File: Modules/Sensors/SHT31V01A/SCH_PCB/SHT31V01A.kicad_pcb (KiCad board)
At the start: 2 copper layers, 40.1 x 9.7 mm, 18 parts, among them J1 CONN1_1, J10 JUMP_2x1, J11 JUMP_2x1, J12 JUMP_2x1, J13 JUMP_2x1, J2 CONN1_1, J9 JUMP_2x1, M1 HOLE, M2 HOLE, U1 SHT31

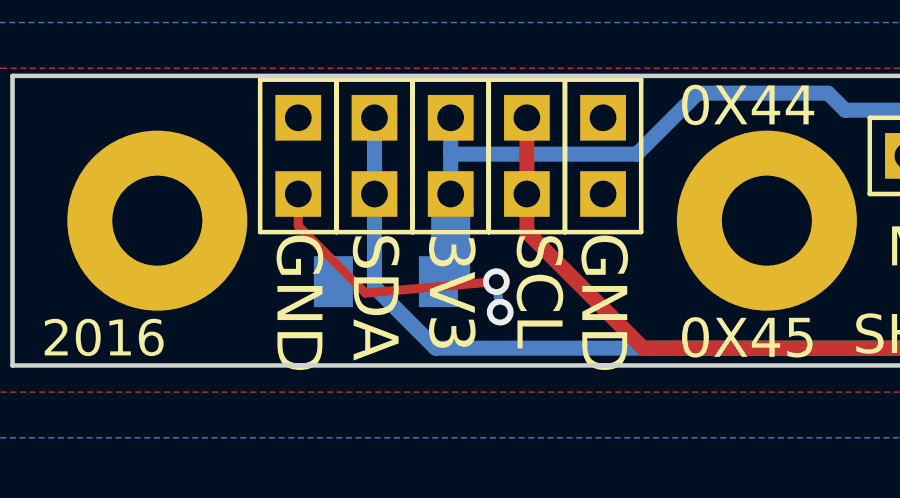
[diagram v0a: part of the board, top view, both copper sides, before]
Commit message: 
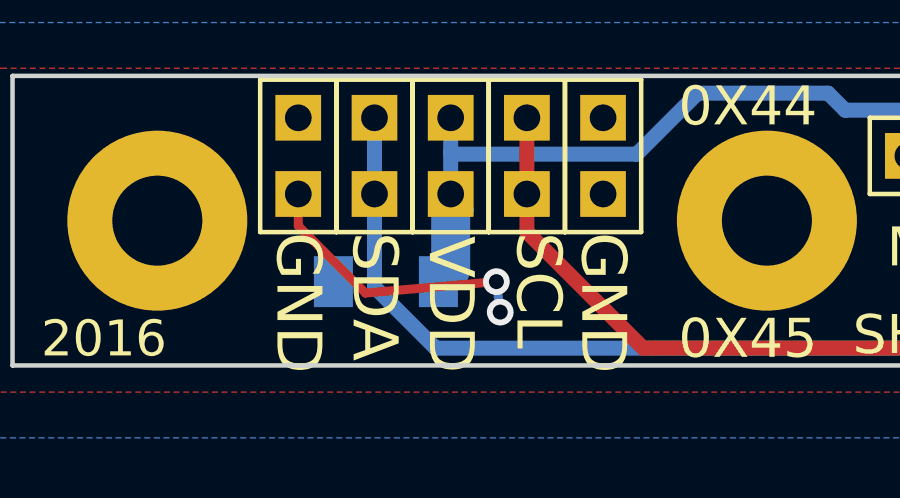
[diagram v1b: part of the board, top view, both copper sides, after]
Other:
- board text added: "VDD"
- board text removed: "3V3"
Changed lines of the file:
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@@
     (links 32)
     (no_connects 0)
-    (area -2.667 -12.524 43.863143 2.159001)
+    (area 0.178999 -9.981001 40.461001 -0.178999)
     (thickness 1.6)
     (drawings 16)
@@
     (effects (font (size 1.5 1.5) (thickness 0.3)) (justify left))
   )
-  (gr_text 3V3 (at 14.859 -4.699 270) (layer F.SilkS)
+  (gr_text VDD (at 14.859 -4.572 270) (layer F.SilkS)
     (effects (font (size 1.5 1.5) (thickness 0.3)) (justify left))
   )

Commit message: 
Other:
- rule pad_to_mask_clearance: 0.2 -> 0.12
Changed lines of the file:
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@@
     (links 32)
     (no_connects 0)
-    (area 0.178999 -9.981001 40.461001 -0.178999)
+    (area -2.667 -12.524 43.863143 2.159001)
     (thickness 1.6)
     (drawings 16)
@@
     (pad_size 1.524 1.524)
     (pad_drill 0.762)
-    (pad_to_mask_clearance 0.2)
+    (pad_to_mask_clearance 0.12)
     (aux_axis_origin 0 0)
     (visible_elements 7FFFFF7F)

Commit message: Nahrani dokumentace
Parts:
- D1: value BZV55C-3,6V -> BZV55C-5,6V
- moved J11 151.2 mm to (137.5, 84.6)
- moved J12 151.2 mm to (129.9, 84.6)
- moved J13 151.2 mm to (140.1, 84.6)
- moved J2 151.2 mm to (158.6, 83.3)
- moved M1 151.2 mm to (145.5, 86.7)
- moved M2 151.2 mm to (125.2, 86.7)
- moved R1 151.2 mm to (151.4, 86.9)
- moved R2 151.2 mm to (155.5, 83.1)
- moved R3 151.2 mm to (159.6, 89.7)
- moved R5 151.2 mm to (152.4, 89.7)
- moved U1 151.2 mm to (157.1, 86.7)
- moved C1 151.2 mm to (153.2, 85.1)
- moved D1 151.2 mm to (132.8, 88.8)
- moved J1 151.2 mm to (150.2, 84.6)
- moved J10 151.2 mm to (132.5, 84.6)
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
